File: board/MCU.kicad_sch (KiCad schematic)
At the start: 23 parts, among them SW1 SW_Push, U1 STSPIN32G4TR

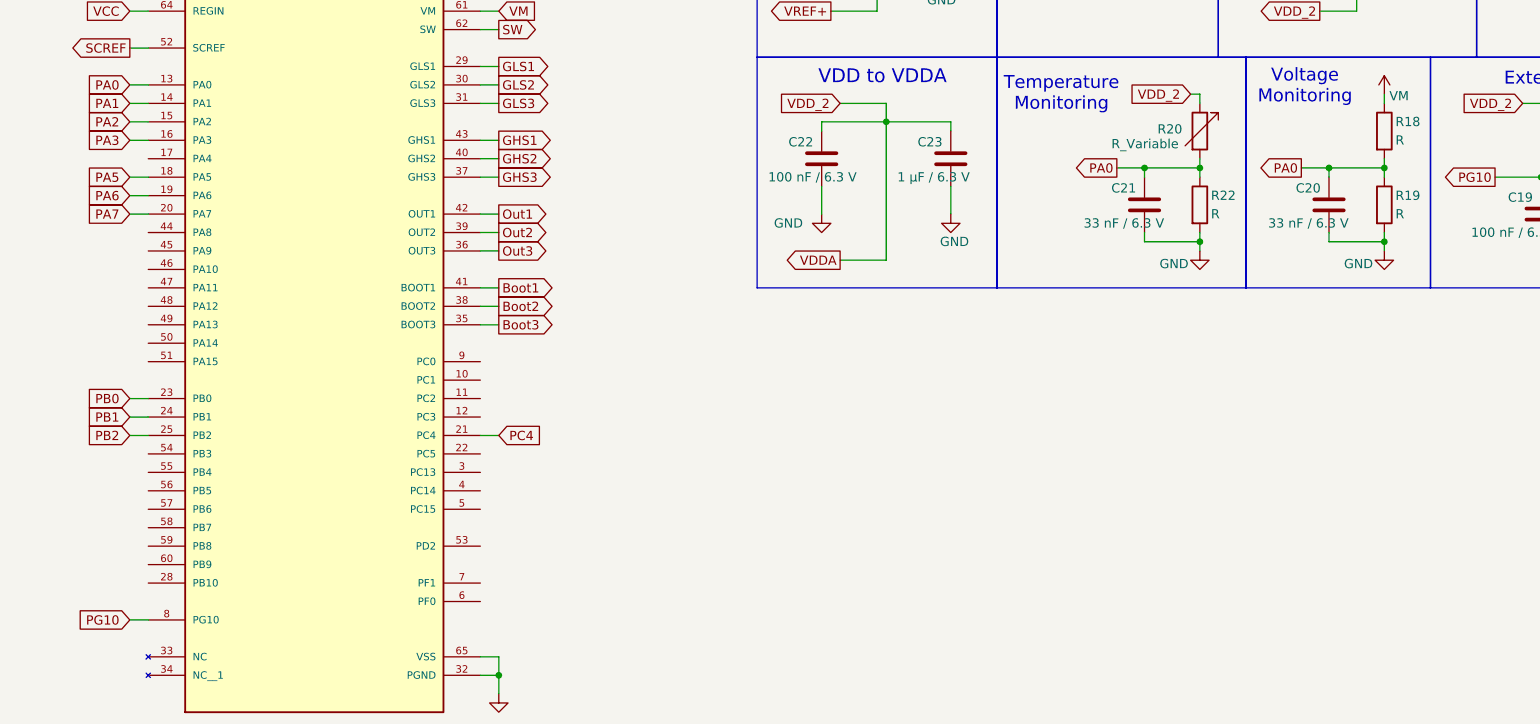
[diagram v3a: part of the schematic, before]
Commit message: Added CAN and Encoder connectors.
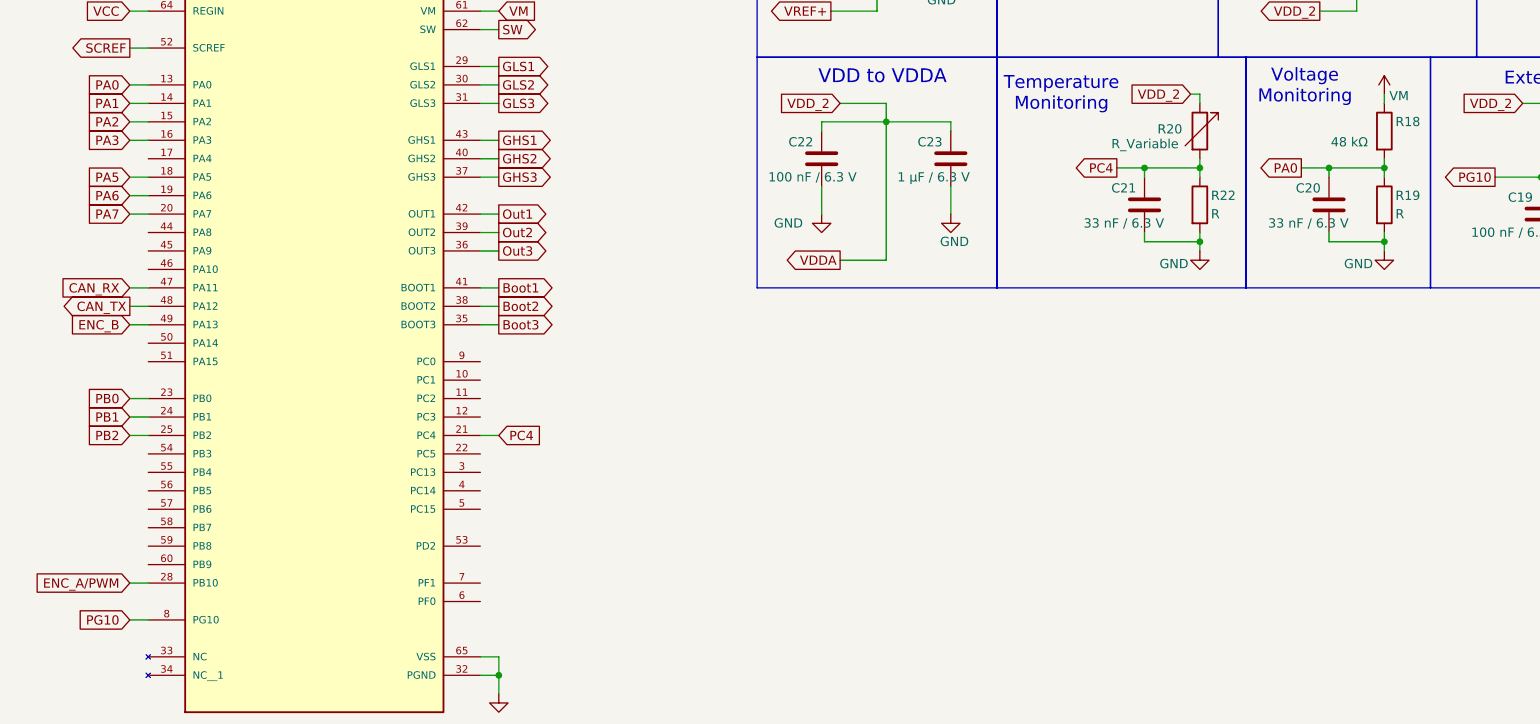
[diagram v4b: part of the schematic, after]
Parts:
- R18: value R -> 48 kΩ
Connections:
- net PA0: no longer C21.1, R20.2, R22.1
- net PC4: now also C21.1, R20.2, R22.1
- net ENC_A/PWM: now reaches U1.28 (PB10)
- net CAN_RX: now reaches U1.47 (PA11)
- net CAN_TX: now reaches U1.48 (PA12)
- net ENC_B: now reaches U1.49 (PA13)
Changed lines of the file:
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@@
 	(wire
 		(pts
+			(xy 38.1 85.09) (xy 40.64 85.09)
+		)
+		(stroke
+			(width 0)
+			(type default)
+		)
+	)
+	(wire
+		(pts
 			(xy 132.08 31.75) (xy 132.08 35.56)
 		)
@@
 	(wire
 		(pts
+			(xy 38.1 82.55) (xy 40.64 82.55)
+		)
+		(stroke
+			(width 0)
+			(type default)
+		)
+	)
+	(wire
+		(pts
 			(xy 203.2 72.39) (xy 203.2 73.66)
 		)
@@
 	(wire
 		(pts
+			(xy 38.1 80.01) (xy 40.64 80.01)
+		)
+		(stroke
+			(width 0)
+			(type default)
+		)
+	)
+	(wire
+		(pts
 			(xy 135.89 76.2) (xy 142.24 76.2)
 		)
@@
 	(wire
 		(pts
+			(xy 38.1 120.65) (xy 40.64 120.65)
+		)
+		(stroke
+			(width 0)
+			(type default)
+		)
+	)
+	(wire
+		(pts
 			(xy 86.36 41.91) (xy 88.9 41.91)
 		)
@@
 		)
 	)
+	(global_label "ENC_B"
+		(shape input)
+		(at 38.1 85.09 180)
+		(fields_autoplaced yes)
+		(effects
+			(font
+				(size 1.27 1.27)
+			)
+			(justify right)
+		)
+		(property "Intersheetrefs" "${INTERSHEET_REFS}"
+			(at 29.1277 85.09 0)
+			(effects
+				(font
+					(size 1.27 1.27)
+				)
+				(justify right)
+				(hide yes)
+			)
+		)
+	)
 	(global_label "Boot2"
 		(shape output)
@@
 		)
 	)
+	(global_label "ENC_A{slash}PWM"
+		(shape input)
+		(at 38.1 120.65 180)
+		(fields_autoplaced yes)
+		(effects
+			(font
+				(size 1.27 1.27)
+			)
+			(justify right)
+		)
+		(property "Intersheetrefs" "${INTERSHEET_REFS}"
+			(at 23.8058 120.65 0)
+			(effects
+				(font
+					(size 1.27 1.27)
+				)
+				(justify right)
+				(hide yes)
+			)
+		)
+	)
 	(global_label "Boot3"
 		(shape output)
@@
 		)
 	)
+	(global_label "CAN_RX"
+		(shape input)
+		(at 38.1 80.01 180)
+		(fields_autoplaced yes)
+		(effects
+			(font
+				(size 1.27 1.27)
+			)
+			(justify right)
+		)
+		(property "Intersheetrefs" "${INTERSHEET_REFS}"
+			(at 27.9786 80.01 0)
+			(effects
+				(font
+					(size 1.27 1.27)
+				)
+				(justify right)
+				(hide yes)
+			)
+		)
+	)
 	(global_label "Out2"
 		(shape output)
@@
 		)
 	)
-	(global_label "PA0"
+	(global_label "PC4"
 		(shape output)
 		(at 173.99 63.5 180)
@@
 		)
 		(property "Intersheetrefs" "${INTERSHEET_REFS}"
-			(at 167.4367 63.5 0)
+			(at 167.2553 63.5 0)
 			(effects
 				(font
@@
 		)
 	)
+	(global_label "CAN_TX"
+		(shape output)
+		(at 38.1 82.55 180)
+		(fields_autoplaced yes)
+		(effects
+			(font
+				(size 1.27 1.27)
+			)
+			(justify right)
+		)
+		(property "Intersheetrefs" "${INTERSHEET_REFS}"
+			(at 28.281 82.55 0)
+			(effects
+				(font
+					(size 1.27 1.27)
+				)
+				(justify right)
+				(hide yes)
+			)
+		)
+	)
 	(global_label "PA2"
 		(shape input)
@@
 			)
 		)
-		(property "Value" "R"
-			(at 212.344 59.69 0)
+		(property "Value" "48 kΩ"
+			(at 203.454 59.944 0)
 			(effects
 				(font

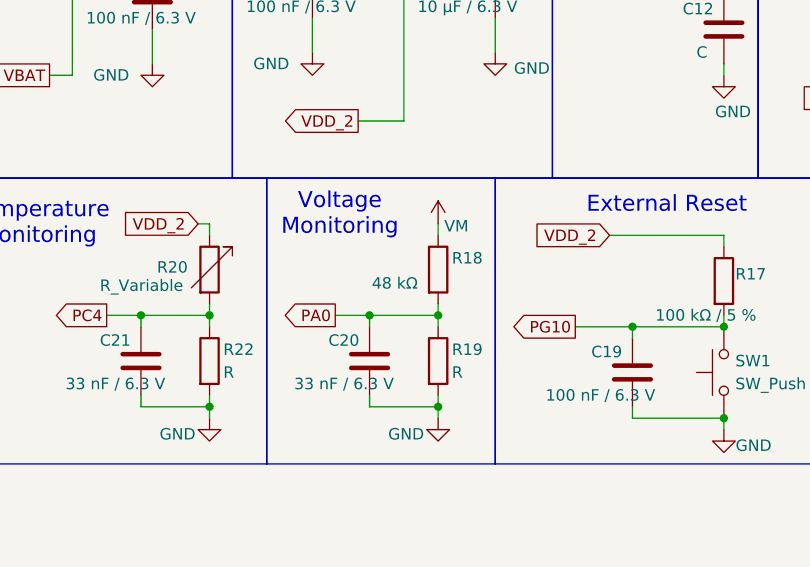
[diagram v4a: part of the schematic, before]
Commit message: Added resistor values to current sense circuit.
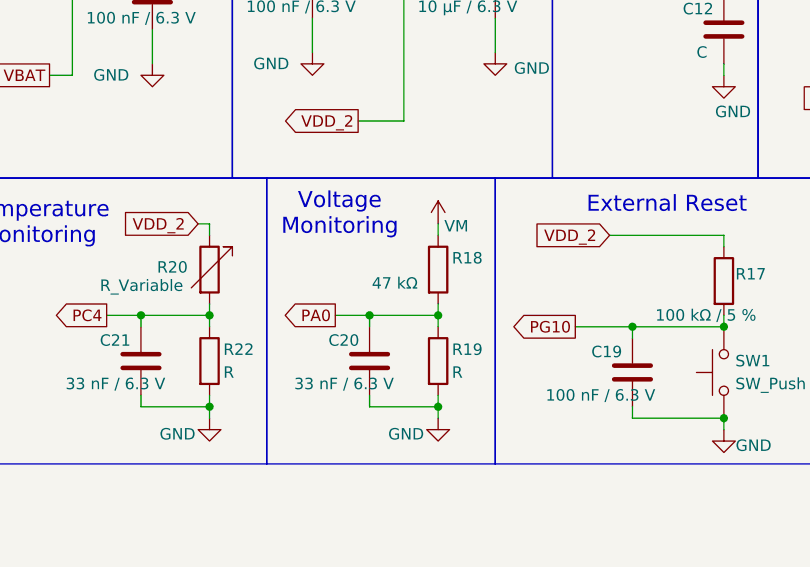
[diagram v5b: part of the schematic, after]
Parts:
- R18: value 48 kΩ -> 47 kΩ
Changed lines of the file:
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@@
 			)
 		)
-		(property "Value" "48 kΩ"
+		(property "Value" "47 kΩ"
 			(at 203.454 59.944 0)
 			(effects

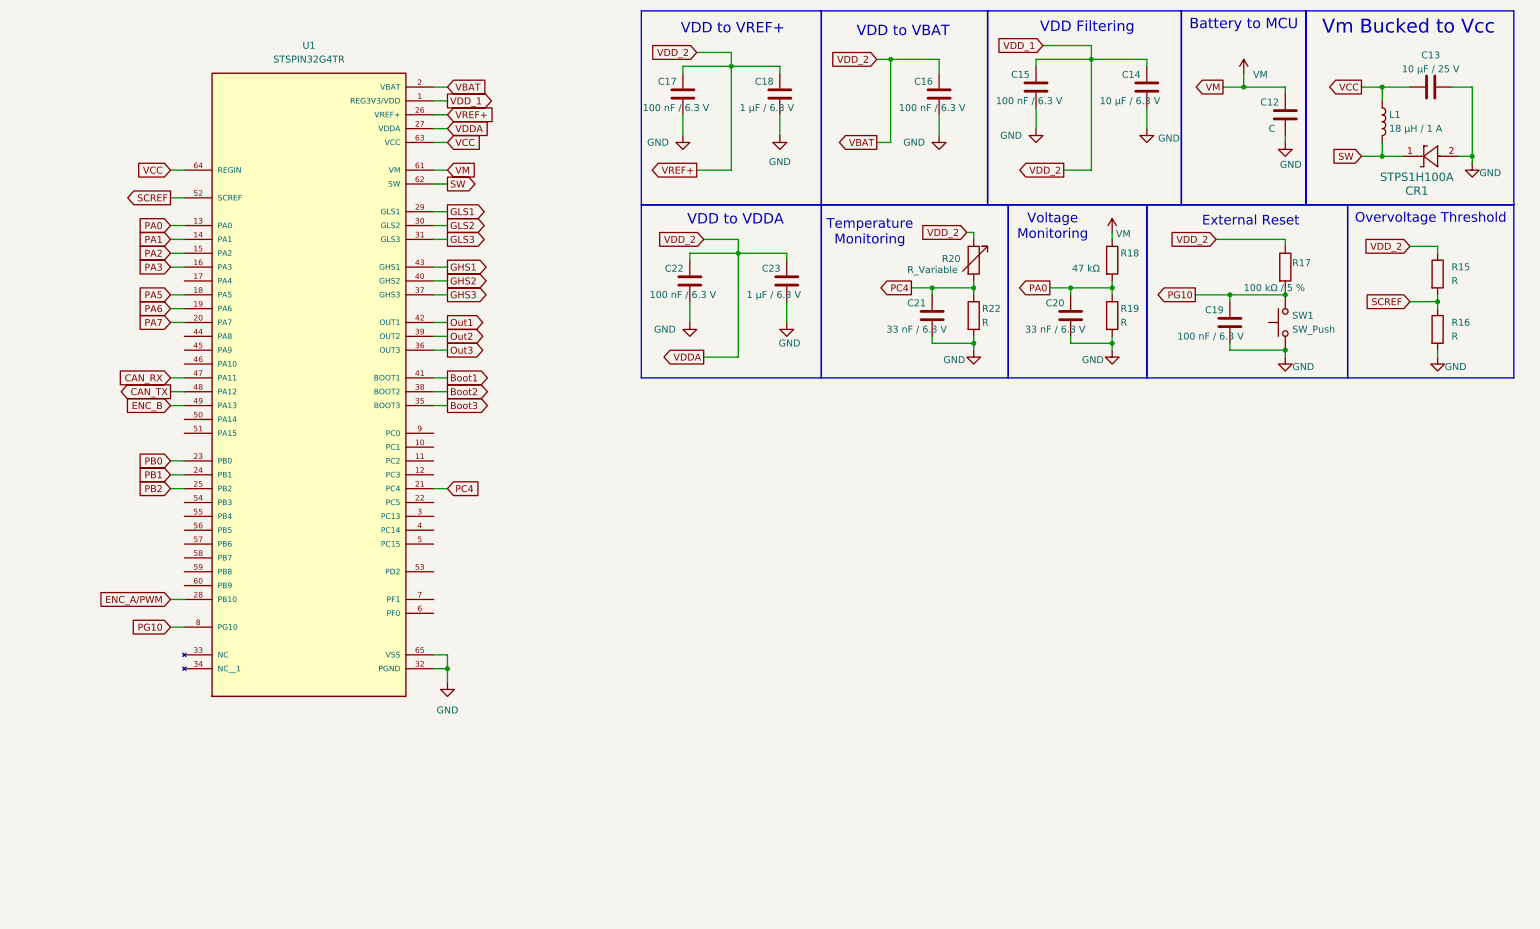
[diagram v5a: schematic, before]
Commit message: Finished adding component values to circuits, except for 4 filtering capacitors
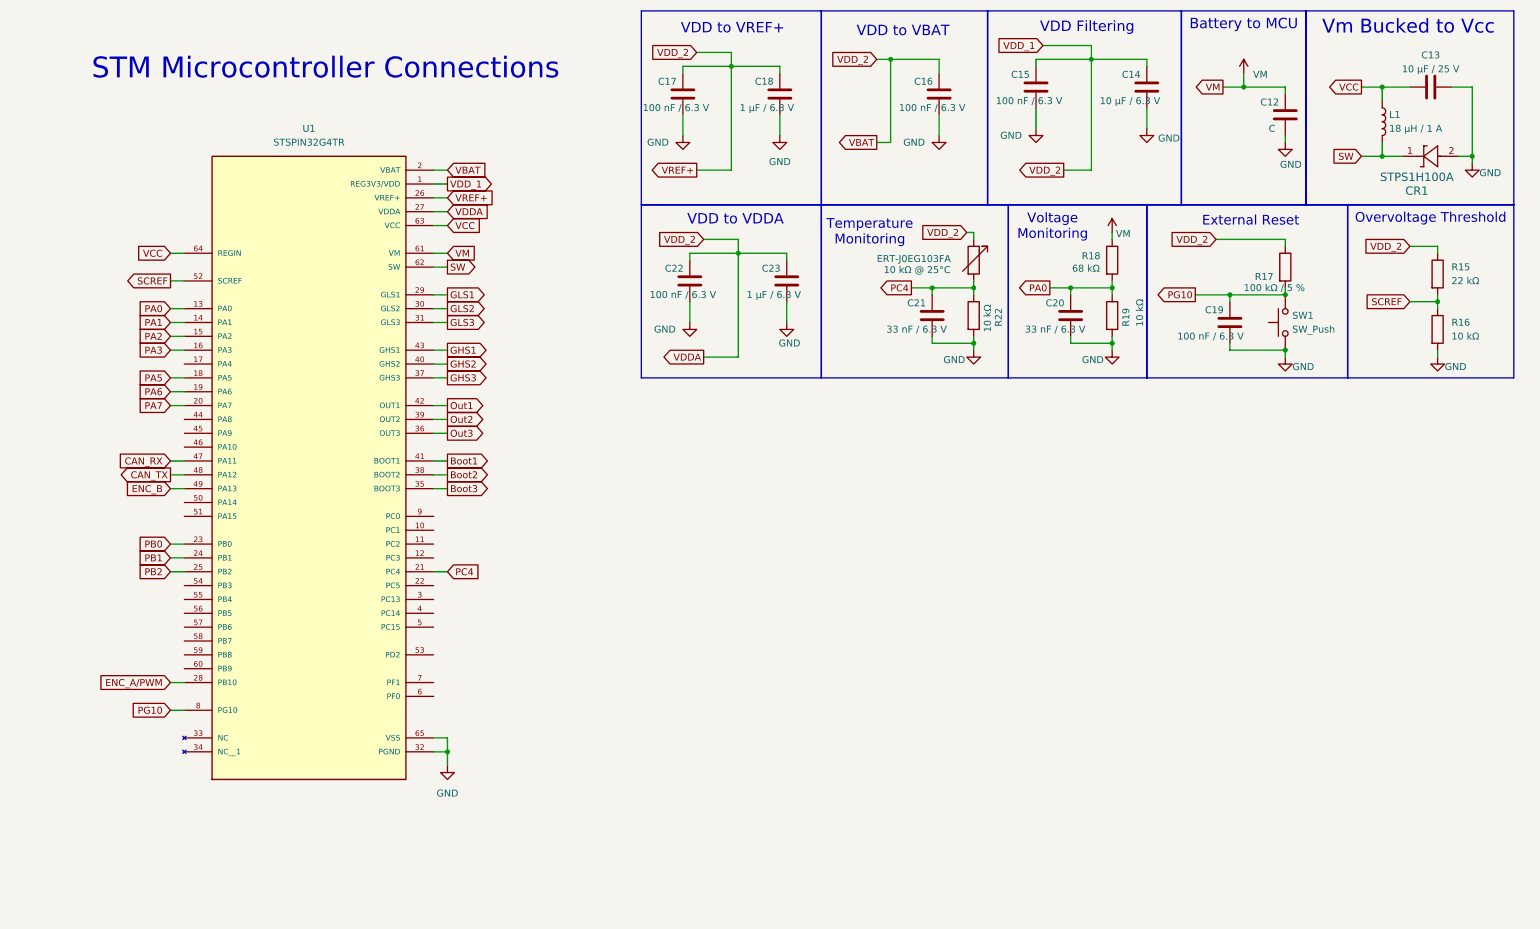
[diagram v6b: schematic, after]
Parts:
- ERT-J0EG103FA: renamed from R20; value R_Variable -> 10 kΩ @ 25°C
- R15: value R -> 22 kΩ
- R16, R19, R22: value R -> 10 kΩ
- R18: value 47 kΩ -> 68 kΩ
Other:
- note added: "STM Microcontroller Connections"
- moved on the sheet: U1

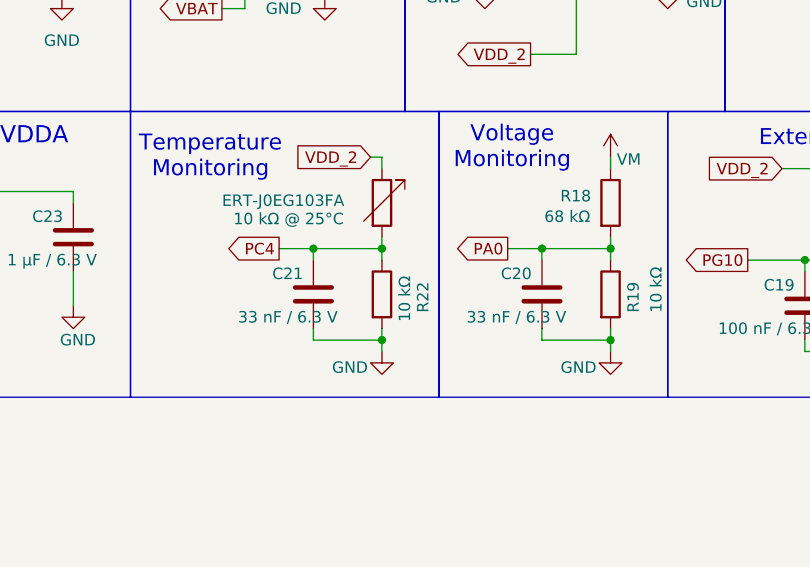
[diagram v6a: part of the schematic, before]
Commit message: Implemented some fixes discussed during the board review.
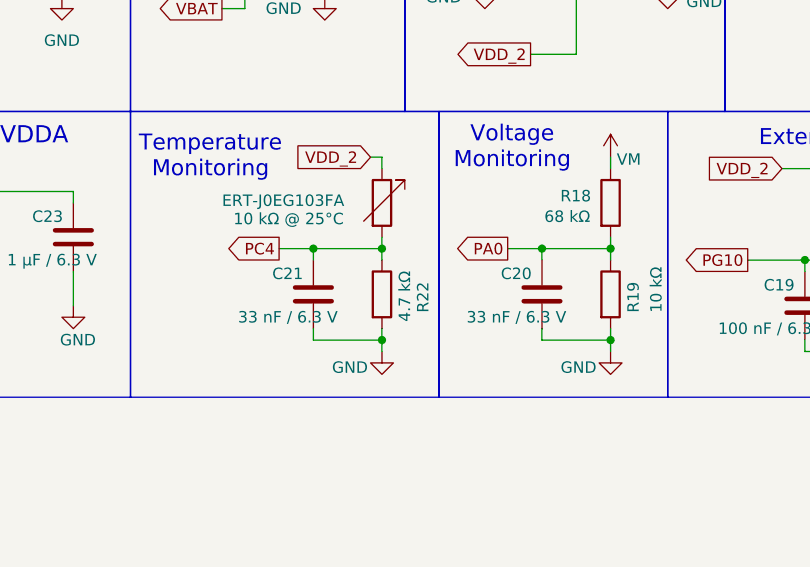
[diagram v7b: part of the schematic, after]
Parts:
- R22: value 10 kΩ -> 4.7 kΩ
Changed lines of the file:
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@@
 			)
 		)
-		(property "Value" "10 kΩ"
+		(property "Value" "4.7 kΩ"
 			(at 187.96 71.628 90)
 			(effects
